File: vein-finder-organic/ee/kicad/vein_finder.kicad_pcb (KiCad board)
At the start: 2 copper layers, 85.7 x 54.4 mm, 65 parts, among them J1 USB-C power-only, Q1 AO3400A, Q2 AO3400A, U1 ATtiny1614, U2 BQ21040DBVR, U3 TPS61169

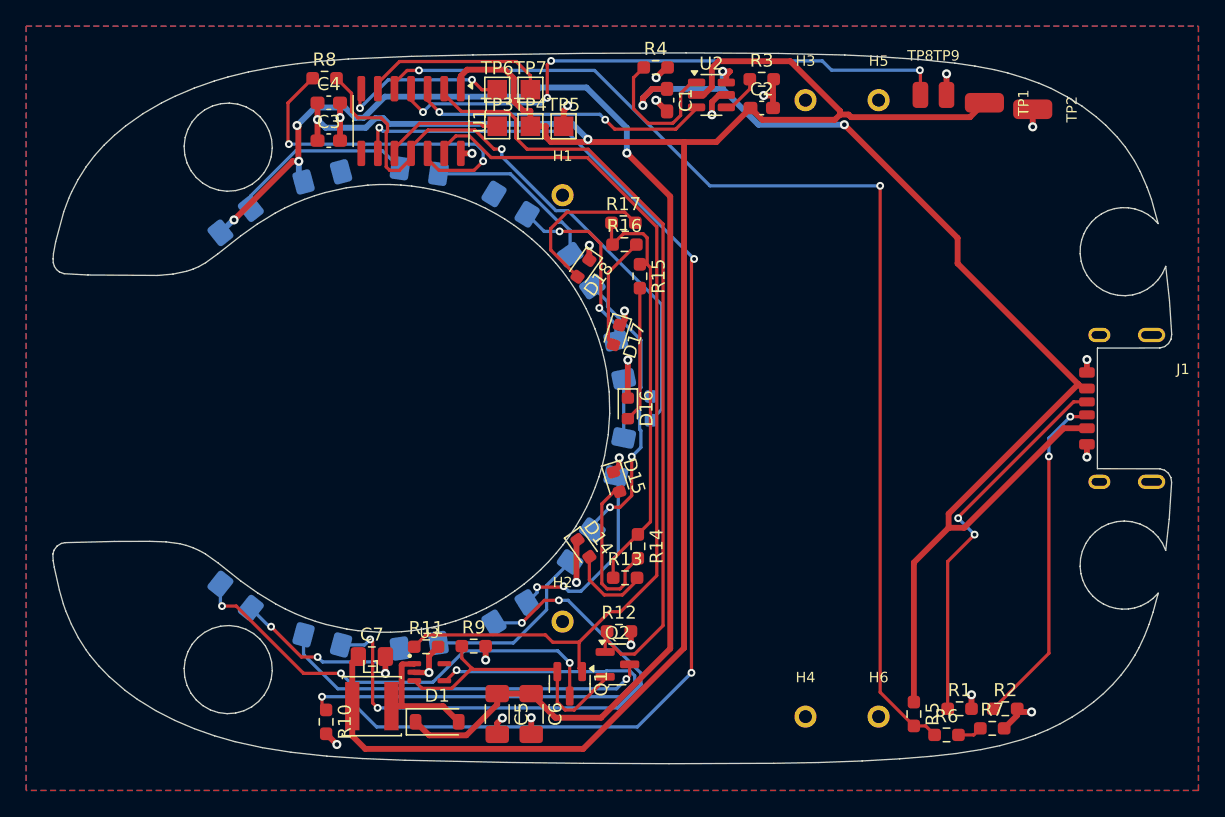
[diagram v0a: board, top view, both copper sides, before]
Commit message: Vein finder (organic): routed PCB, DRC clean (0 errors, 0 unconnected)
- fix top-side footprint orientation (KiCad angle = device CCW angle on both
  sides); pad positions now checked against the intended transform
- fix project file being reset to KiCad defaults (no throwaway BOARD())
- U3/D1/C7 turned so the boost loop is compact (VIN next to C7)
- GND routed as its own 0.3 mm net class; pours added after routing
- finish_route.py: rip-up-and-reroute finisher (grid A*, exact clearance
  checks, transactional rollback), edge/clearance violators re-routed,
  GND islands stitched by connectivity
- silk.py: references placed clear of pads/silk/edge, test pads labelled
  with their function, edge silk clipped; project fp-lib-table and a
  .kicad_dru for the USB-C and outer ring-LED lands
- Gerbers, drill, positions and PDFs in docs/03-electronics/fab

Co-Authored-By: Claude Opus 5.5 <noreply@anthropic.com>
Claude-Session: https://claude.ai/code/session_01VQzXs58X1YYUn6JuF7hh2E
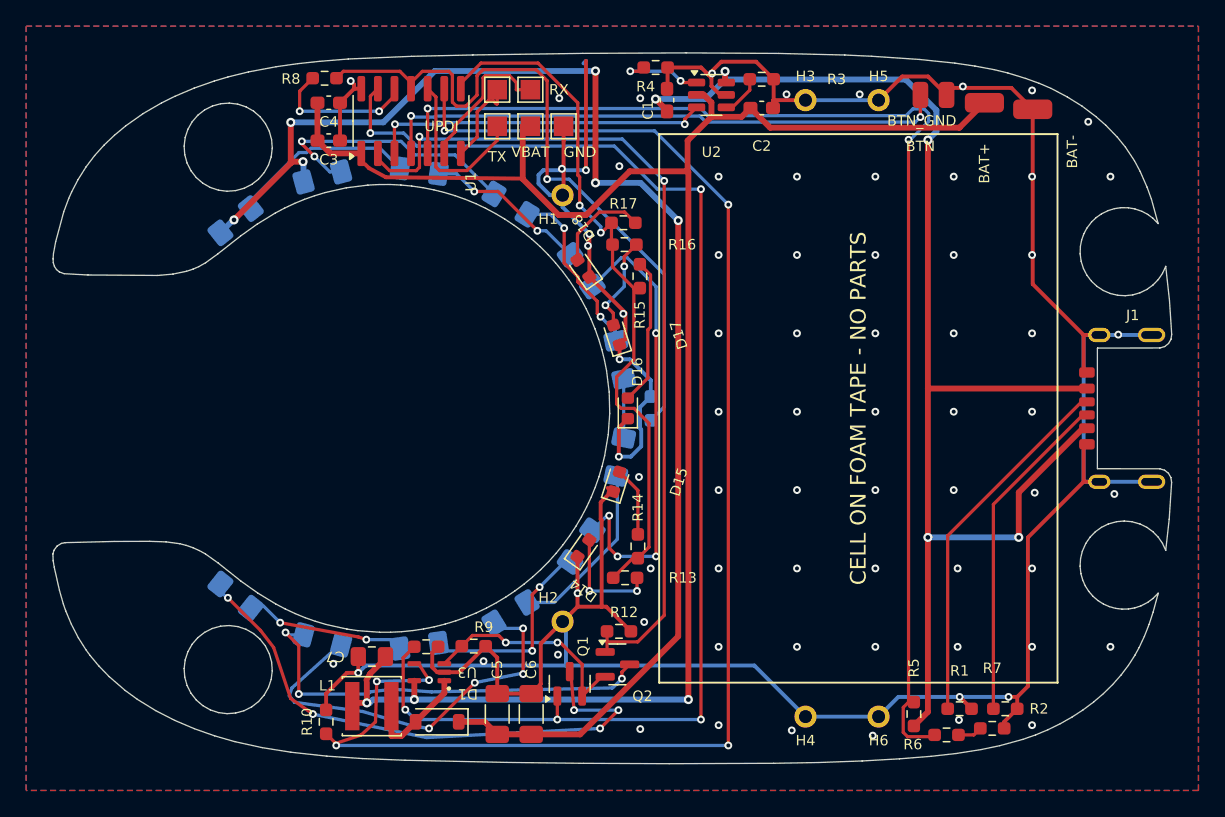
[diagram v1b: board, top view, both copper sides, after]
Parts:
- turned C1 to 90 degrees
- turned C5 to 90 degrees
- turned C6 to 90 degrees
- turned C7 to 180 degrees
- turned D1 to 180 degrees
- turned D14 to 54.8 degrees
- turned D15 to 72.4 degrees
- turned D16 to 90 degrees
- turned D17 to 107.6 degrees
- turned D18 to 125.2 degrees
- turned Q1 to 90 degrees
- turned R10 to 90 degrees
- turned R14 to 90 degrees
- turned R15 to 90 degrees
- turned R5 to 90 degrees
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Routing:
- net GND: track 42.6 -> 266.0 mm, vias 25 -> 72
- net GATE_A: track 70.3 -> 101.3 mm, vias 0 -> 5
- net SEAM_PWM: track 32.7 -> 54.9 mm, vias 0 -> 2
- net VBAT: track 161.7 -> 139.6 mm, vias 2 -> 3
- net LED_CTRL: track 132.3 -> 111.7 mm, vias 5 -> 6
- net B1: track 0.00 -> 20.5 mm, vias 0 -> 2
- net NTC_EN: track 27.1 -> 11.2 mm
- net B5: track 44.0 -> 30.2 mm
- net A3: track 22.3 -> 35.4 mm, vias 2 -> 4
- net VBUS: track 94.4 -> 103.6 mm, vias 3 -> 5
- net VBUS_SENSE: track 86.0 -> 93.6 mm
- net STR_A: track 34.7 -> 41.8 mm, vias 3 -> 5
- net SEAM2: track 12.3 -> 5.35 mm
- net DBG_TX: track 13.3 -> 6.75 mm, vias 2 -> 0
- net NTC_SENSE: track 47.6 -> 53.6 mm
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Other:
- board text added: "CELL ON FOAM TAPE - NO PARTS"

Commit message: Vein finder (organic): outer ring LEDs pulled in to clear the 0.3 mm edge rule
- layout: the two end LEDs move from +-128.5 to +-126.1 deg (tested on the real
  roundrect pads against the outline as cut: 0.312 mm); the other ten keep
  their places, so the sole over every dome is unchanged
- PCB re-routed; DRC 0 errors, 0 unconnected; the D2/D7 DRC exception is gone
  (only the USB-C datasheet land pattern keeps one)
- finish_route: prune stubs of no length and vias that join only one layer

Co-Authored-By: Claude Opus 5.5 <noreply@anthropic.com>
Claude-Session: https://claude.ai/code/session_01VQzXs58X1YYUn6JuF7hh2E
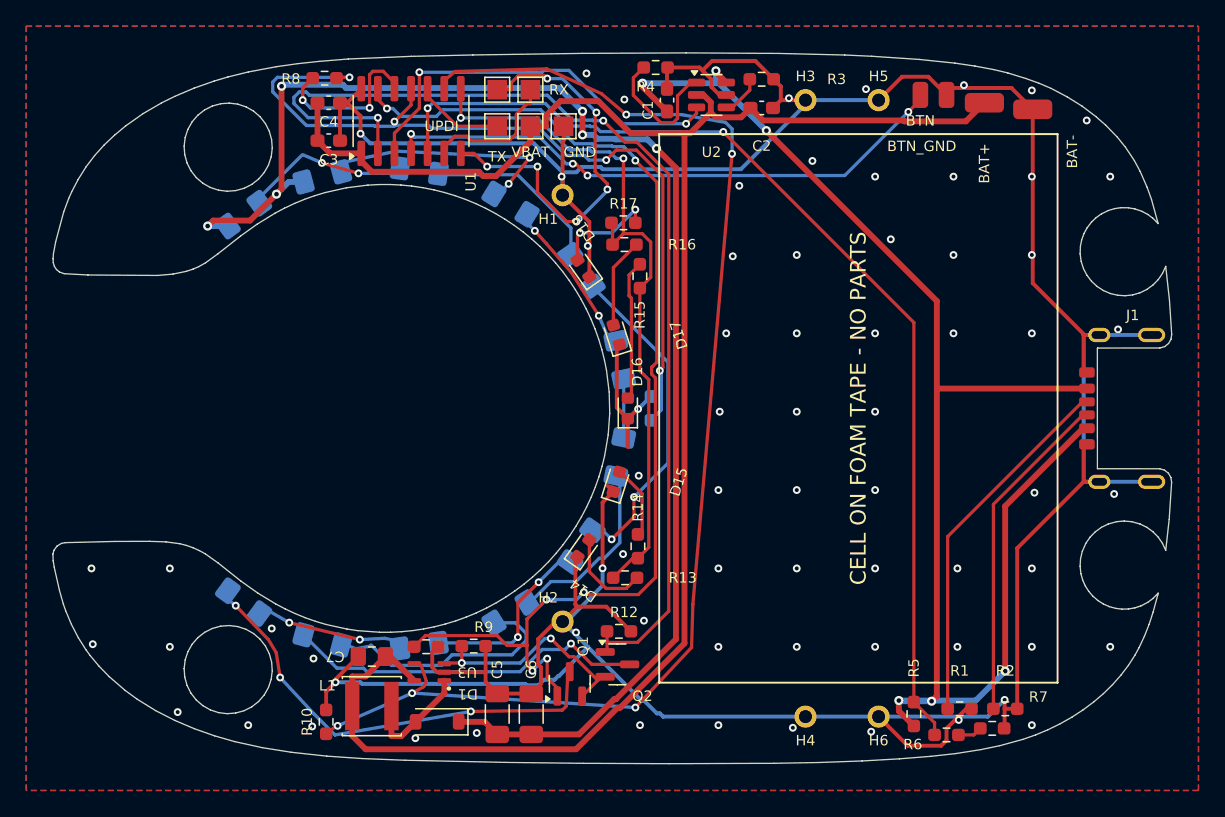
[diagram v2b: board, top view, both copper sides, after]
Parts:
- moved D2 0.77 mm to (99.2, 85.2), turned to -143.9 degrees
- moved D7 0.77 mm to (99.2, 114.8), turned to -36.1 degrees
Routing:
- net GND: track 266.0 -> 295.3 mm, vias 72 -> 71
- net DBG_TX: track 6.75 -> 31.5 mm, vias 0 -> 6
- net GATE_A: track 101.3 -> 85.3 mm, vias 5 -> 6
- net LED_CTRL: track 111.7 -> 96.0 mm, vias 6 -> 5
- net GATE_B: track 66.7 -> 82.4 mm
- net VBUS_SENSE: track 93.6 -> 80.0 mm
- net B5: track 30.2 -> 18.3 mm, vias 4 -> 0
- net A3: track 35.4 -> 25.3 mm, vias 4 -> 2
- net NTC_SENSE: track 53.6 -> 63.5 mm, vias 1 -> 4
- net VBUS: track 103.6 -> 112.2 mm, vias 5 -> 6
- net STR_A: track 41.8 -> 33.3 mm, vias 5 -> 3
- net UPDI: track 13.1 -> 6.88 mm
- net STR_B: track 32.9 -> 27.7 mm, vias 3 -> 1
- net CHG_STAT: track 26.2 -> 30.8 mm
- net TS: track 6.58 -> 10.5 mm, vias 2 -> 0
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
